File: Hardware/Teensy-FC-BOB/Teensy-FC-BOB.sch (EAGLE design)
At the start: 1 part

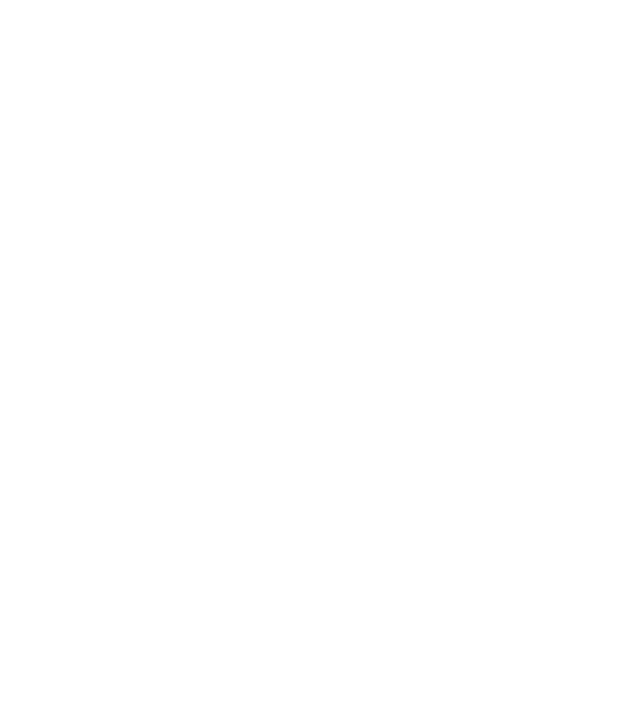
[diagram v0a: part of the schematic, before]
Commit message: decided to make this a dual teensy flight controller break out
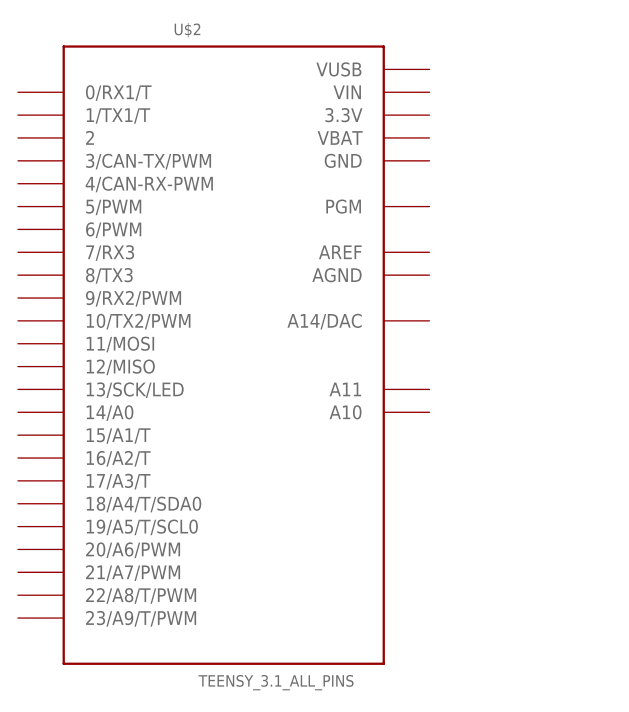
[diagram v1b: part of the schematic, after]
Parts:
- added U$2: TEENSY_3.1_ALL_PINS, Teensy_3_and_LC_Series_Boards_v1.0:TEENSY_3.1_ALL_PINS
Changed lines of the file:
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@@
 <parts>
 <part name="U$1" library="Teensy_3_and_LC_Series_Boards_v1.0" deviceset="TEENSY_3.1_ALL_PINS" device=""/>
+<part name="U$2" library="Teensy_3_and_LC_Series_Boards_v1.0" deviceset="TEENSY_3.1_ALL_PINS" device=""/>
 </parts>
 <sheets>
@@
 <instances>
 <instance part="U$1" gate="G$1" x="134.62" y="116.84"/>
+<instance part="U$2" gate="G$1" x="17.78" y="116.84"/>
 </instances>
 <busses>

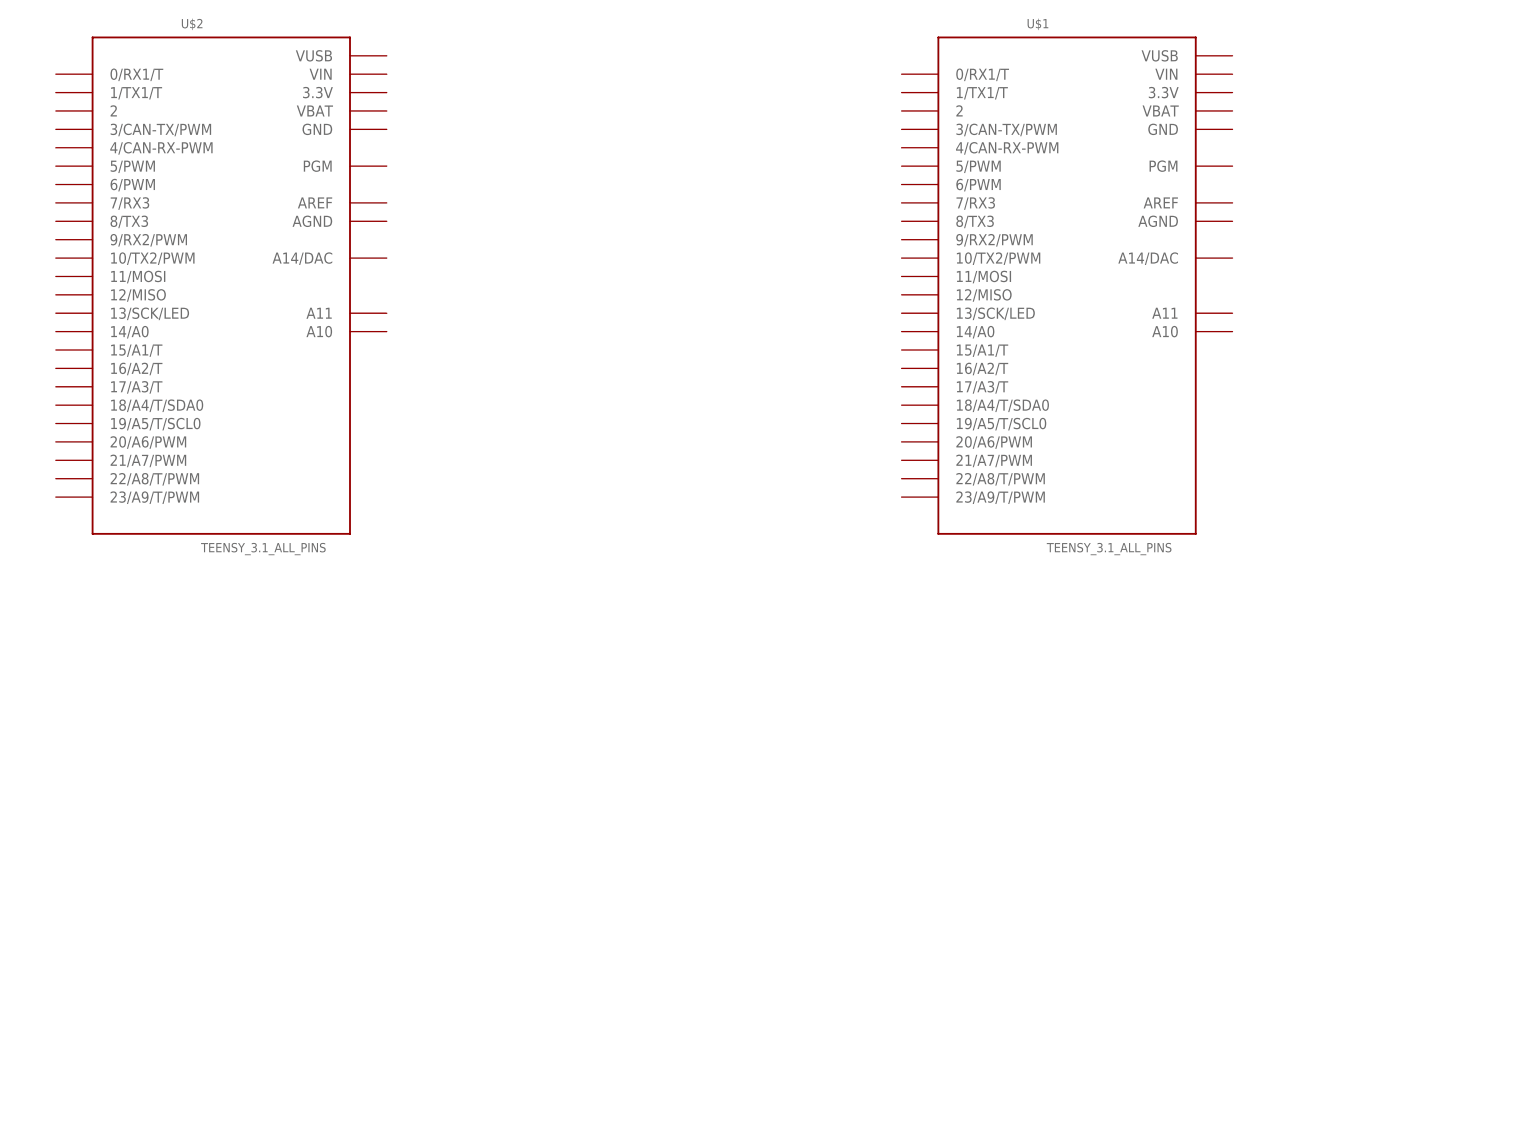
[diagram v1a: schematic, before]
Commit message: added the 10dof to the bob
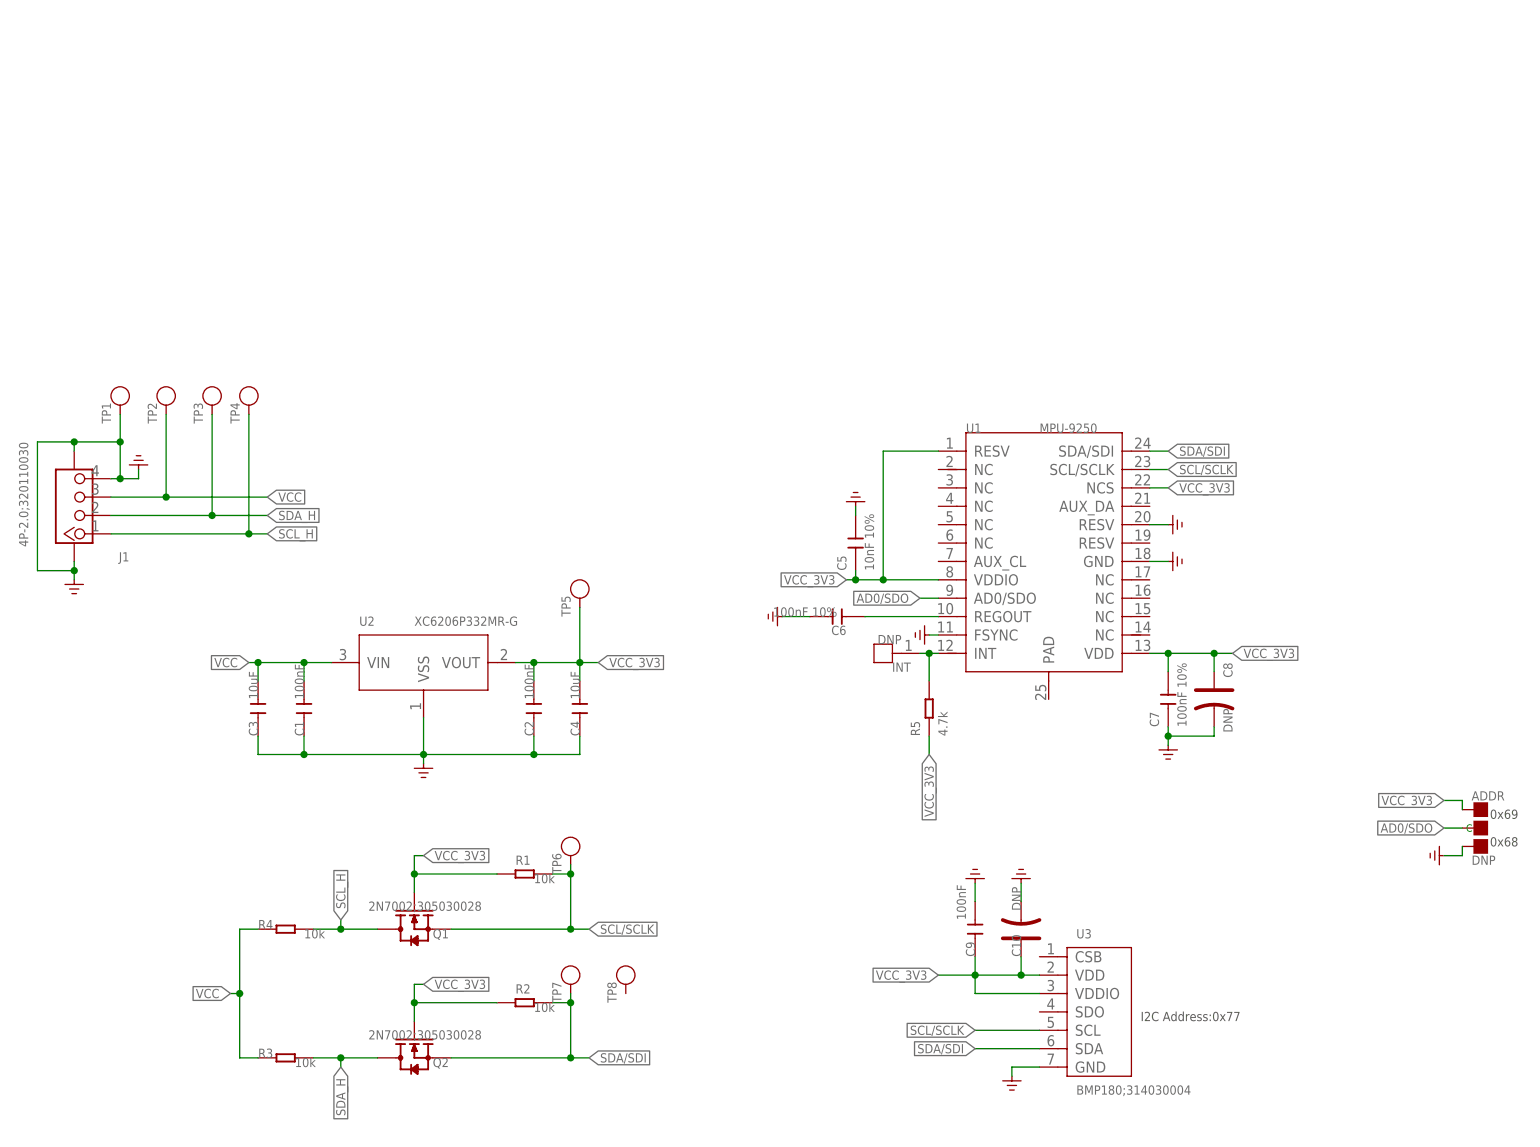
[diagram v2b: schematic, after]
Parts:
- removed U$1, U$2: TEENSY_3.1_ALL_PINS, Teensy_3_and_LC_Series_Boards_v1.0:TEENSY_3.1_ALL_PINS
- added ADDR: DNP, Discrete-new:PAD-JUMPER-3P-40*40
- added C1, C2, C9: 100nF, Discrete-new:CAP-0603
- added C10, C8: DNP, Discrete-new:CAP-POLAR-AVX-A
- added C3, C4: 10uF, Discrete-new:CAP-0805
- added C5: 10nF 10%, Discrete-new:CAP-0603
- added C6, C7: 100nF 10%, Discrete-new:CAP-0603
- added INT: DNP, Connector-new:HEADER-1P-35
- added J1: 4P-2.0;320110030, Connector-new:GROVE-CONNECTOR-SMD'DD'
- added Q1, Q2: 2N7002;305030028, Discrete-new:MOSFET-N'SOT23'
- added R1, R2, R3, R4: 10k, Discrete-new:RES-0603
- added R5: 4.7k, Discrete-new:RES-0603
- added TP1, TP2, TP3, TP4, TP5, TP6, TP7, TP8: DNP, Discrete-new:PAD-TEST-POINT'4545'
- added U1: MPU-9250, template:MPU-9250
- added U2: XC6206P332MR-G, IC-new:PMIC-XC6206PMR
- added U3: BMP180;314030004, template:BMP180
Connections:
- new net AD0/SDO: ADDR.C, U1.AD0/SDO
- new net GND: ADDR.R, C1.1, C10.-, C2.1, C3.1, C4.1, C5.2, C6.2, C7.1, C8.-, C9.2, J1.4, J1.SS1, J1.SS2, TP1.T, U1.FSYNC, U1.GND, U1.RESV@2, U2.VSS, U3.GND
- new net N$3: C6.1, U1.REGOUT
- new net N$4: INT.1, R5.2, U1.INT
- new net SCL/SCLK: Q1.S, R1.2, TP6.T, U1.SCL/SCLK, U3.SCL
- new net SCL_H: J1.1, Q1.D, R4.2, TP4.T
- new net SDA/SDI: Q2.S, R2.2, TP7.T, U1.SDA/SDI, U3.SDA
- new net SDA_H: J1.2, Q2.D, R3.2, TP3.T
- new net VCC: C1.2, C3.2, J1.3, R3.1, R4.1, TP2.T, U2.VIN
- new net VCC_3V3: ADDR.L, C10.+, C2.2, C4.2, C5.1, C7.2, C8.+, C9.1, Q1.G, Q2.G, R1.1, R2.1, R5.1, TP5.T, U1.NCS, U1.RESV, U1.VDD, U1.VDDIO, U2.VOUT, U3.VDD, U3.VDDIO
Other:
- note added: "0x68"
- note added: "0x69"
- note added: "I2C Address:0x77"
